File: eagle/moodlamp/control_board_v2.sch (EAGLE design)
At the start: 38 parts, among them IC1 MEGA8-AI, J1 POWER_JACKPTH, Q1 N-HEXFET-2D_SOT232-IRLL014N, Q2 N-HEXFET-2D_SOT232-IRLL014N, Q3 N-HEXFET-2D_SOT232-IRLL014N

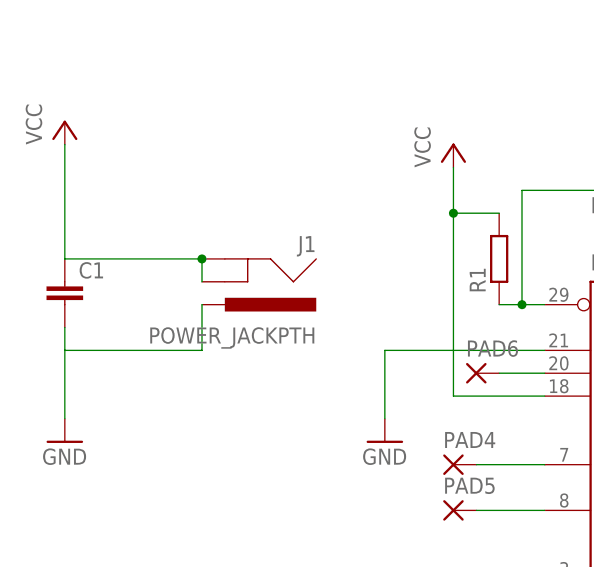
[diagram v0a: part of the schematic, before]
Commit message: power jack fixed
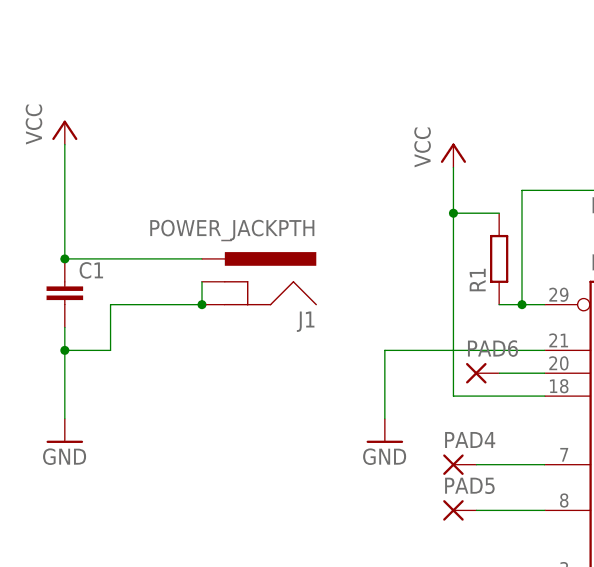
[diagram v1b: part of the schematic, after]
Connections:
- net GND: now also J1.GND, J1.GNDBREAK; no longer J1.PWR
- net VCC: now also J1.PWR; no longer J1.GND, J1.GNDBREAK
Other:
- moved on the sheet: J1
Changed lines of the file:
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@@
 <instances>
 <instance part="IC1" gate="G$1" x="55.88" y="58.42"/>
-<instance part="J1" gate="G$1" x="-2.54" y="91.44" rot="R180"/>
+<instance part="J1" gate="G$1" x="-2.54" y="81.28" rot="MR0"/>
 <instance part="C1" gate="G$1" x="-20.32" y="86.36"/>
 <instance part="C2" gate="G$1" x="20.32" y="50.8"/>
@@
 <pinref part="GND1" gate="1" pin="GND"/>
 <wire x1="-20.32" y1="81.28" x2="-20.32" y2="78.74" width="0.1524" layer="91"/>
-<pinref part="J1" gate="G$1" pin="PWR"/>
+<pinref part="J1" gate="G$1" pin="GND"/>
 <wire x1="-20.32" y1="78.74" x2="-20.32" y2="71.12" width="0.1524" layer="91"/>
-<wire x1="-5.08" y1="83.82" x2="-5.08" y2="78.74" width="0.1524" layer="91"/>
-<wire x1="-5.08" y1="78.74" x2="-20.32" y2="78.74" width="0.1524" layer="91"/>
+<wire x1="-5.08" y1="83.82" x2="-15.24" y2="83.82" width="0.1524" layer="91"/>
+<wire x1="-15.24" y1="83.82" x2="-15.24" y2="78.74" width="0.1524" layer="91"/>
+<wire x1="-15.24" y1="78.74" x2="-20.32" y2="78.74" width="0.1524" layer="91"/>
+<junction x="-20.32" y="78.74"/>
+<pinref part="J1" gate="G$1" pin="GNDBREAK"/>
+<wire x1="-5.08" y1="86.36" x2="-5.08" y2="83.82" width="0.1524" layer="91"/>
+<junction x="-5.08" y="83.82"/>
 </segment>
 <segment>
@@
 <pinref part="C1" gate="G$1" pin="1"/>
 <wire x1="-20.32" y1="101.6" x2="-20.32" y2="88.9" width="0.1524" layer="91"/>
-<pinref part="J1" gate="G$1" pin="GND"/>
+<pinref part="J1" gate="G$1" pin="PWR"/>
 <wire x1="-5.08" y1="88.9" x2="-20.32" y2="88.9" width="0.1524" layer="91"/>
-<pinref part="J1" gate="G$1" pin="GNDBREAK"/>
-<wire x1="-5.08" y1="86.36" x2="-5.08" y2="88.9" width="0.1524" layer="91"/>
-<junction x="-5.08" y="88.9"/>
+<junction x="-20.32" y="88.9"/>
 </segment>
 <segment>

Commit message: v2 prototype
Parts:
- added D1, D2: 3V6, diode:ZENER-DIODESOD80C
- added R6: 1k5, resistor:R-EU_R0805
- added R7, R8: 68R, resistor:R-EU_R0805
- C1, C2: device resistor:C-EUC1206 -> resistor:C-EUC0805
- PAD1, PAD2, PAD20, PAD21, PAD22, PAD3: value WIREPADSMD5-2,5 -> (none); device wirepad:WIREPADSMD5-2,5 -> wirepad:2,54/1,0
- R1, R2, R3, R4, R5: device resistor:R-EU_R1206 -> resistor:R-EU_R0805
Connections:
- new net N$30: D1.C, R6.2, R7.2, USB1.2
- new net N$31: D2.C, R8.2, USB1.3
- net +5V: now also R6.1
- net GND: now also D1.A, D2.A
- net N$10: now also IC1.PD1(TXD), R7.1; no longer IC1.PD6(AIN0), USB1.2
- net N$11: now also IC1.PD2(INT0), R8.1; no longer IC1.PD7(AIN1), USB1.3
- net N$24: now also IC1.PD4(XCK/T0); no longer IC1.PD1(TXD)
- net N$25: now also IC1.PD7(AIN1); no longer IC1.PD4(XCK/T0)
- net N$8: now also IC1.PD6(AIN0), S2.2.1; no longer IC1.PD2(INT0), S1.2.1
- net N$9: now also S1.2.1; no longer S2.2.1
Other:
- moved on the sheet: PAD16, PAD17, USB1

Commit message: Silkscreen
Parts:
- PAD20, PAD21, PAD22: value (none) -> LED+
- renumbered JP1 to ISP, PAD1 to RED, PAD16 to P16, PAD2 to GRN, PAD3 to BLU, Q1 to T1, Q2 to T2, Q3 to T3, USB1 to USB
